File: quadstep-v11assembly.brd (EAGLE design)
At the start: 100 x 50 mm, 127 parts, among them IC2 PIC18F2455_28W, U1 A4983, U2 A4983, U3 A4983, U4 A4983, X1 MSTBA4, X10 22-23-2041, X11 MSTBA4, X2 MSTBA4, X3 MSTBA4, X4 MSTBA4, X6 ICSP-5, X7 22-23-2041, X8 22-23-2041, X9 22-23-2041

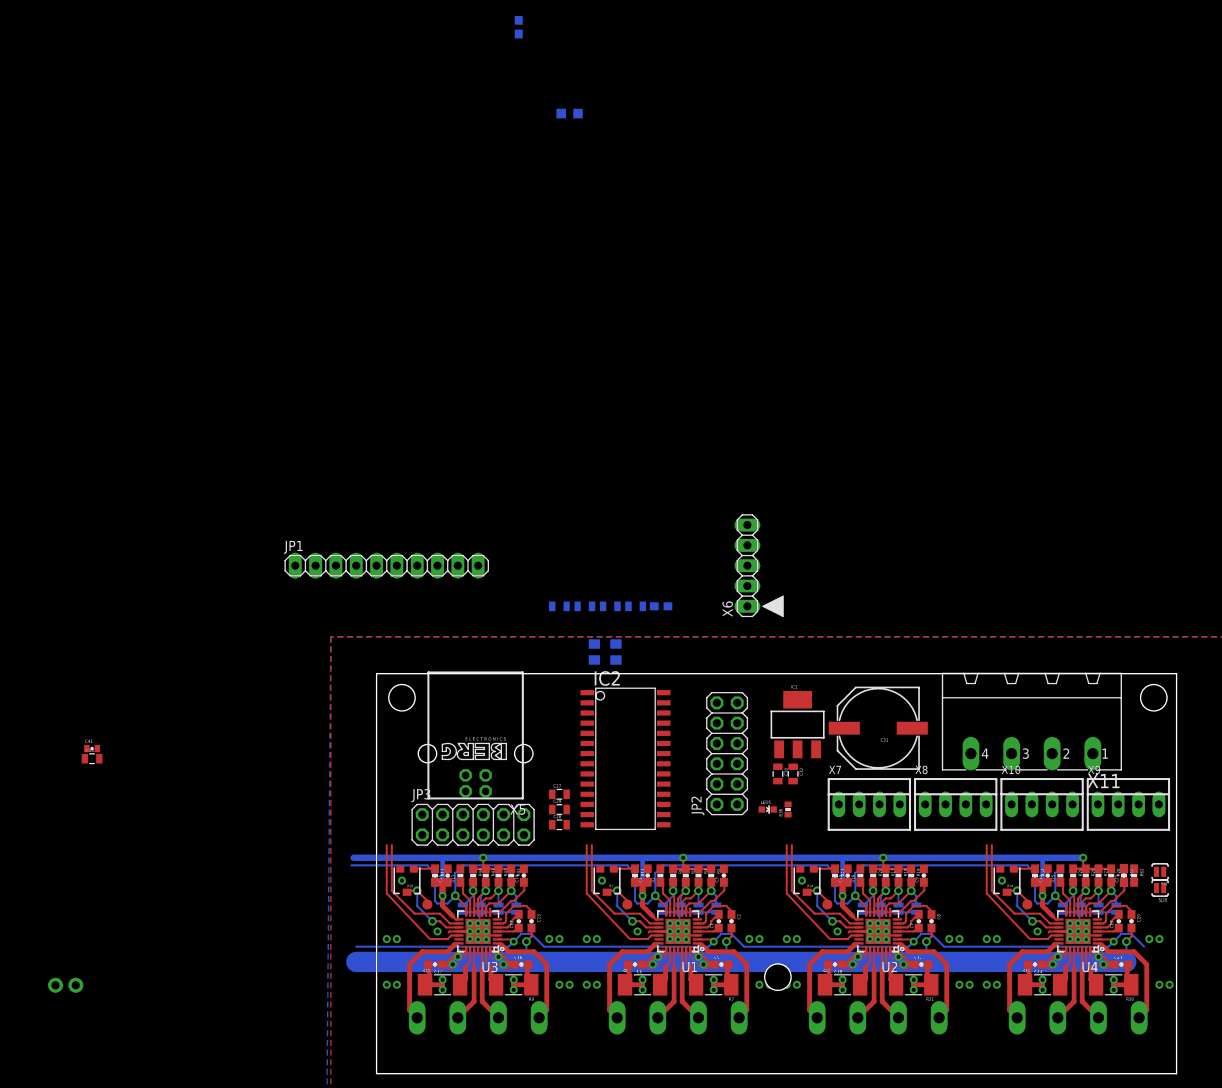
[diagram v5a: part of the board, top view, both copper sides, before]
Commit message: Layout with new TQFP IC
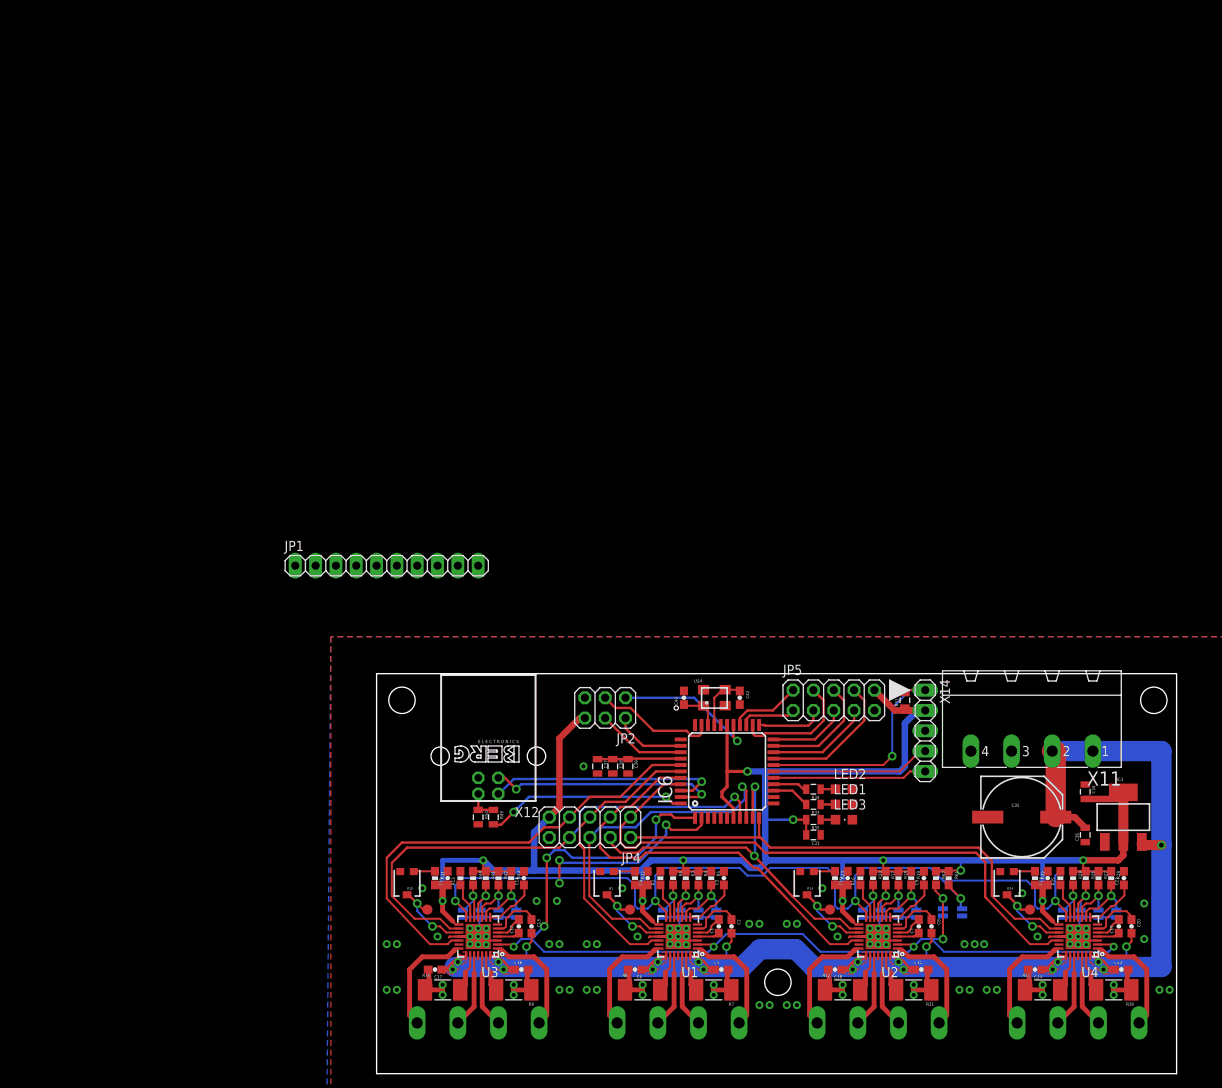
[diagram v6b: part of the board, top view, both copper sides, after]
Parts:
- removed C25, C26: 8pF, SparkFun:0603-CAP
- removed C27, C28, C29, C32: 100nF, SparkFun:0805
- removed C30: 10uF, SparkFun:0805
- removed C31: 470uF, SparkFun:PANASONIC_G
- removed C41: 0.1uF, SparkFun:0402-CAP
- removed C44: 1uF, SparkFun:0805
- removed IC1: (no value), SparkFun:SOT223
- removed IC2: PIC18F2455_28W, microchip:SO28W
- removed JP21: (no value), SparkFun:1X02
- removed JP3: (no value), pinhead:2X06
- removed LED5: red, SparkFun:LED-0603
- removed R36: 330, SparkFun:0402-RES
- removed R37: 10k, SparkFun:0805
- removed U$6: CRYSTAL-SMD- 12MHz, crystal:CRYSTAL-SMD-3.2X2.5
- removed X10, X7, X8, X9: 22-23-2041, con-molex:22-23-2041
- removed X5: (no value), con-berg:PN61729
- removed X6: ICSP-5, ICSP:M05
- added C33: 10uF, SparkFun:0805
- added C34, C36, C37, C38, C39: 100nF, SparkFun:0805
- added C35: 470uF, SparkFun:PANASONIC_G
- added C40, C42: 8pF, SparkFun:0603-CAP
- added IC3: NCP1117ST50T3G, SparkFun:SOT223
- added IC6: PIC18F4550_TQFP, microchip:TQFP44
- added JP4, JP5: (no value), pinhead:2X05
- added LED2, LED3: (no value), led:CHIPLED_0805
- added R49, R50, R51: 10k, SparkFun:0805
- added U$4: CRYSTAL-SMD- 12MHz, crystal:CRYSTAL-SMD-3.2X2.5
- added X12: USB B, con-berg:PN61729
- added X14: ICSP-5, ICSP:M05
- JP2: device pinhead:2X06 -> pinhead:2X03
- moved LED1 92.9 mm to (58.4, 33.7), flipped to the top
- moved R33 40.3 mm to (54.6, 33.7), flipped to the top
- moved R35 36.8 mm to (54.6, 31.8), flipped to the top
- moved R34 36.6 mm to (54.6, 35.6), flipped to the top
- moved SJ26 27.3 mm to (70.8, 20.2), flipped to the bottom, turned to 90 degrees
- moved SJ1 25.3 mm to (73.2, 20.2), flipped to the bottom, turned to 90 degrees
- moved R62 24.8 mm to (69.9, 24.4)
- moved R61 21.9 mm to (71.5, 24.4)
- moved JP2 16.3 mm to (28.6, 45.7), turned to 180 degrees
- moved TP3 0.71 mm to (81.7, 20.5)
- moved TP1 0.71 mm to (31.7, 20.5)
- moved TP2 0.71 mm to (56.7, 20.5)
- moved C1 0.64 mm to (42.8, 18.4)
- moved C12 0.64 mm to (17.8, 18.4)
- moved C13 0.64 mm to (19.4, 18.4)
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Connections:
- removed net LED: R33.2
- removed net VDD: IC2.20, R34.1, X6.2
- new net LED1: IC6.14, R33.2
- new net LED2: IC6.15, R34.2
- new net N$65: IC6.19, JP5.8
- new net N$66: IC6.20, JP5.7
- new net N$67: IC6.21, JP5.6
- new net N$68: IC6.22, JP5.5
- new net N$69: IC6.23, JP5.3
- new net N$70: IC6.24, JP5.4
- new net N$71: IC6.25, JP5.1
- new net N$72: IC6.26, JP5.2
- new net N$73: LED2.A, R34.1
- new net N$74: IC6.35, JP2.2
- new net N$75: IC6.36, JP2.4
- new net N$76: IC6.32, JP2.3
- new net N$77: IC6.27, JP2.1
- net !MCLR: now also IC6.18, R51.2, X14.1; no longer IC2.1, R34.2, X6.1
- net D+: now also IC6.43, X12.3; no longer IC2.16, X5.3
- net D-: now also IC6.42, X12.2; no longer IC2.15, X5.2
- net DIR-1: now also IC6.38, JP4.7
- net DIR-2: now also IC6.39, JP4.5
- net DIR-3: now also IC6.40, JP4.3
- net DIR-4: now also IC6.41, JP4.1
- net EN: now also IC6.1
- net GND: now also C33.1, C34.1, C35.-, C36.1, C37.2, C38.2, C39.2, C40.2, C42.2, IC3.1, IC6.29, IC6.6, JP2.5, JP4.10, JP5.9, LED2.C, LED3.C, R50.2, U$4.2, U$4.4, X12.4, X14.3; no longer C25.2, C26.2, C27.1, C28.1, C29.1, C30.1, C31.-, C32.1, C41.2, C44.2, IC1.1, IC2.19, IC2.8, JP21.2, R36.1, R37.2, U$6.2, U$6.4, X5.4, X6.3
- net N$27: now also LED3.A, R35.1; no longer LED5.C, R36.2
- net OSC1: now also C42.1, IC6.30, U$4.3; no longer C26.1, IC2.9, U$6.3
- net OSC2: now also C40.1, IC6.31, U$4.1; no longer C25.1, IC2.10, U$6.1
- net PGC: now also IC6.16, X14.5; no longer IC2.27, X6.5
- net PGD: now also IC6.17, X14.4; no longer IC2.28, X6.4
- net SLP: now also IC6.2
- net STP-1: now also IC6.8, JP4.8
- net STP-2: now also IC6.9, JP4.6
- net STP-3: now also IC6.10, JP4.4
- net STP-4: now also IC6.11, JP4.2
- net USB_SENSE: now also IC6.44, R49.2; no longer IC2.22, R35.2
- net VBUS: now also R49.1, R50.1, X12.1; no longer R35.1, R37.1, X5.1
- net VCC: now also C35.+, C36.2, IC3.3, X11.1, X11.2; no longer C31.+, C32.2, IC1.3, JP21.1
- net VOUT: now also C33.2, C34.2, IC3.2, IC3.4, IC6.28, IC6.7, JP2.6, JP4.9, JP5.10, R35.2, R51.1, X14.2; no longer C30.2, C41.1, C44.1, IC1.2, IC1.4, LED5.A
- net VUSB: now also C37.1, C38.1, C39.1, IC6.37; no longer C27.2, C28.2, C29.2, IC2.14
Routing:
- net VOUT: track 196.6 -> 301.6 mm, vias 8 -> 11
- net DIR-4: track 17.7 -> 75.4 mm
- net STP-1: track 15.8 -> 64.5 mm, vias 0 -> 1
- net STP-4: track 15.8 -> 63.3 mm
- net DIR-1: track 17.7 -> 58.3 mm
- net DIR-3: track 17.7 -> 53.4 mm
- net STP-3: track 15.8 -> 49.6 mm, vias 0 -> 2
- net VCC: track 246.3 -> 276.1 mm, vias 20 -> 21
- net !MCLR: track 0.00 -> 29.6 mm, vias 0 -> 1
- net D+: track 0.00 -> 29.6 mm, vias 0 -> 2
- net D-: track 0.00 -> 29.4 mm, vias 0 -> 1
- net STP-2: track 15.8 -> 44.9 mm, vias 0 -> 1
- net USB_SENSE: track 0.00 -> 25.3 mm, vias 0 -> 2
- net EN: track 112.4 -> 133.6 mm, vias 4 -> 9
- net PGD: track 0.00 -> 20.0 mm
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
